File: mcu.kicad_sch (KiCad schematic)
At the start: 2 parts, among them U1 nRF52840

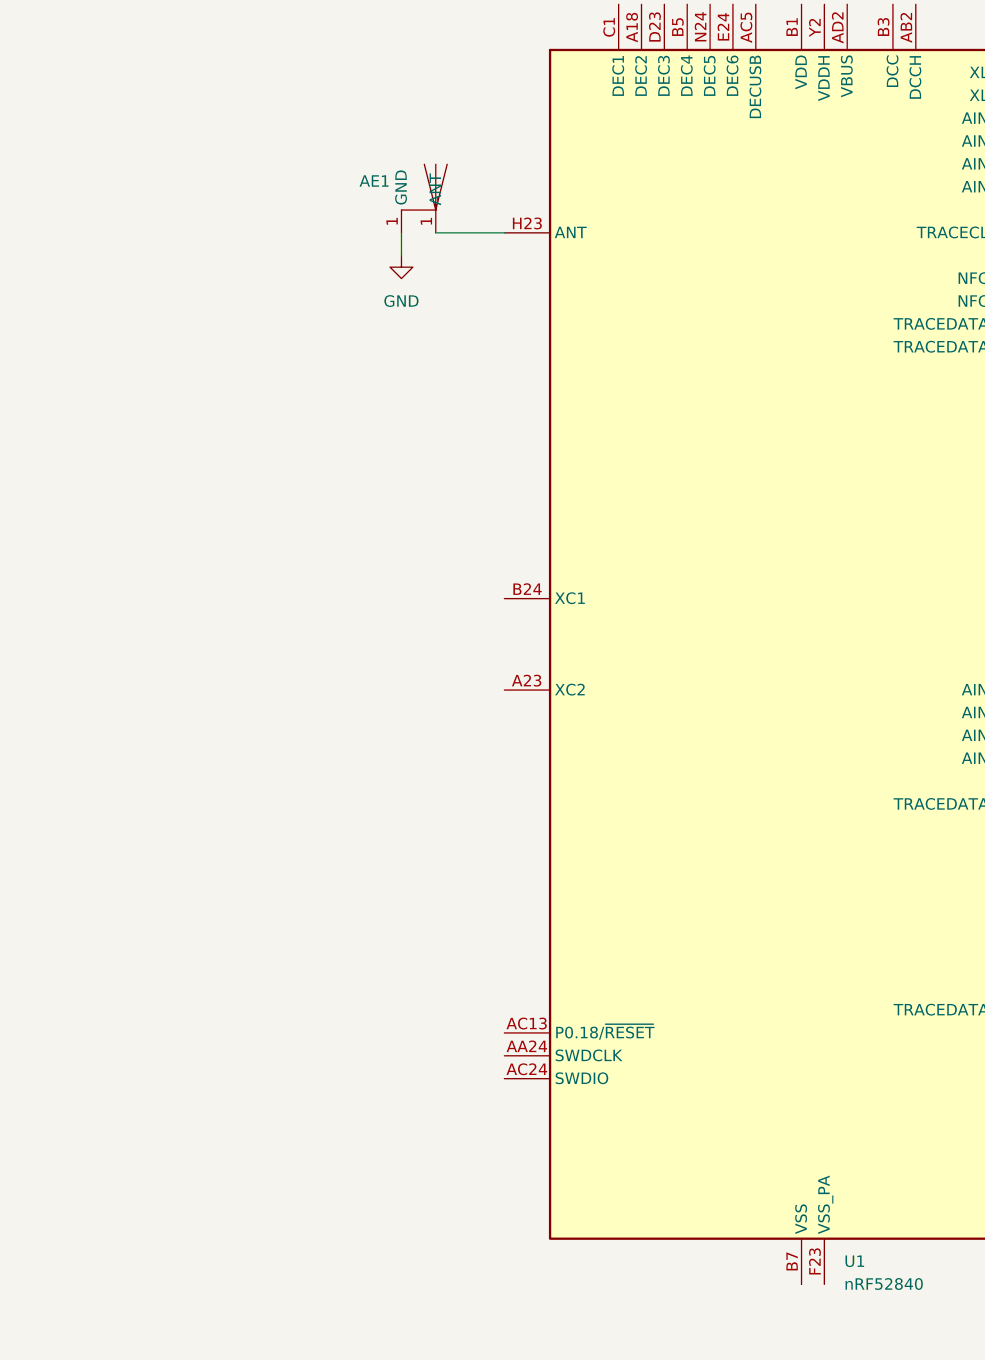
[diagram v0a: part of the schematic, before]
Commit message: Added antenna
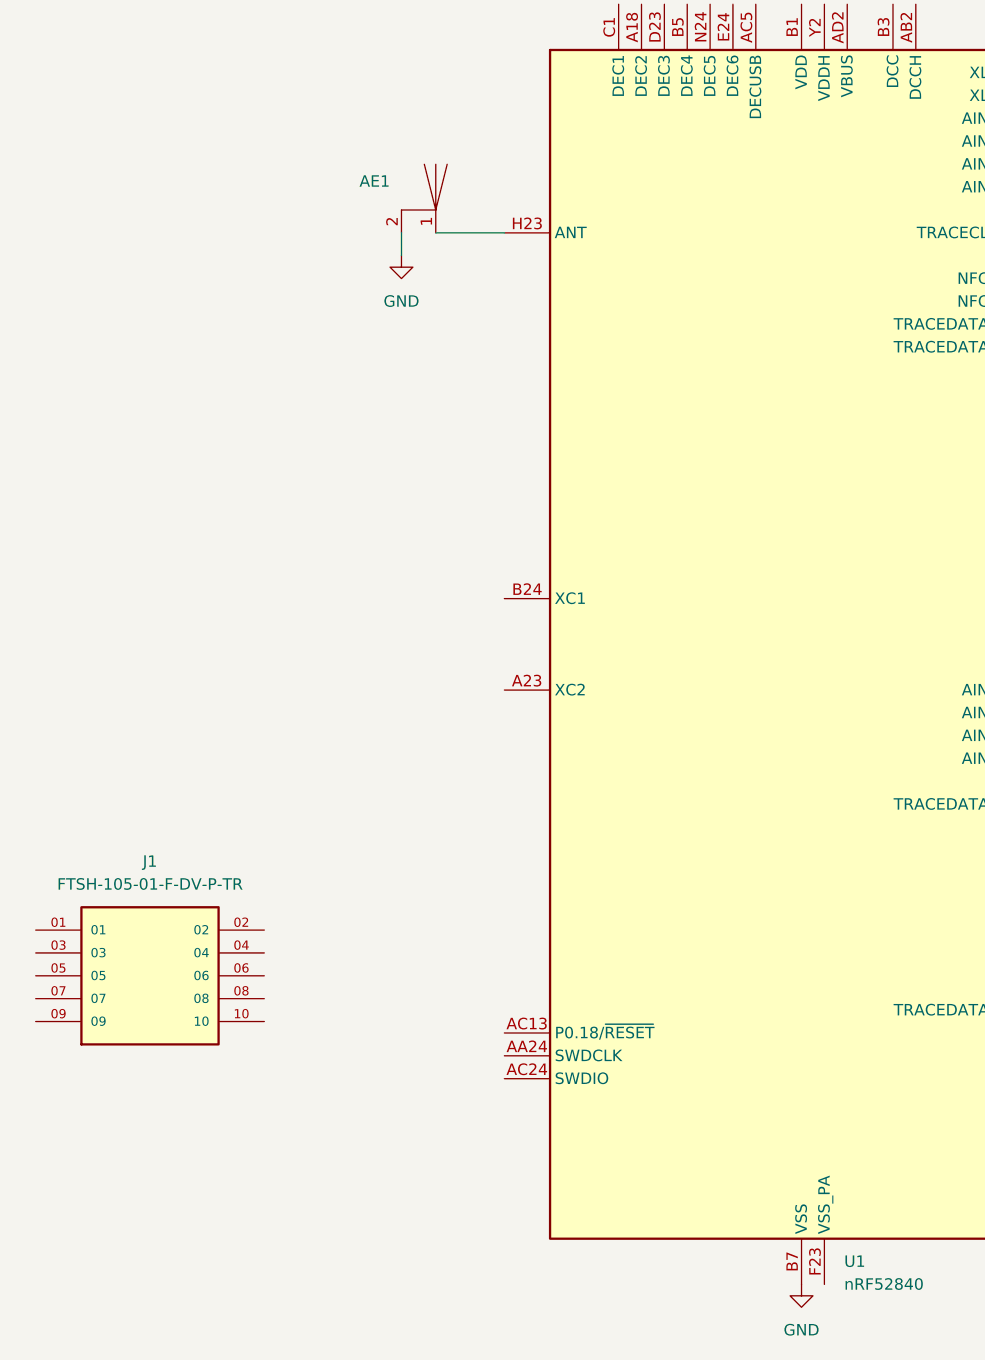
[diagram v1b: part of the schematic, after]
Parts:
- added J1: FTSH-105-01-F-DV-P-TR, Personal:SAMTEC_FTSH-105-01-F-DV-P-TR, symbol FTSH-105-01-F-DV-P-TR:FTSH-105-01-F-DV-P-TR
- AE1: now left out of the parts list
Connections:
- net GND: now also AE1.2, U1.B7 (VSS), U1.EP (VSS); no longer AE1.1 (GND)
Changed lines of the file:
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@@
+	)
+	(symbol
+		(lib_id "FTSH-105-01-F-DV-P-TR:FTSH-105-01-F-DV-P-TR")
+		(at 53.34 135.89 0)
+		(unit 1)
+		(exclude_from_sim no)
+		(in_bom yes)
+		(on_board yes)
+		(dnp no)
+		(fields_autoplaced yes)
+		(property "Reference" "J1"
+			(at 53.34 123.19 0)
+			(effects
+				(font
+					(size 1.27 1.27)
+				)
+			)
+		)
+		(property "Value" "FTSH-105-01-F-DV-P-TR"
+			(at 53.34 125.73 0)
+			(effects
+				(font
+					(size 1.27 1.27)
+				)
+			)
+		)
+		(property "Footprint" "Personal:SAMTEC_FTSH-105-01-F-DV-P-TR"
+			(at 53.34 135.89 0)
+			(effects
+				(font
+					(size 1.27 1.27)
+				)
+				(justify bottom)
+				(hide yes)
+			)
+		)
+		(property "Datasheet" ""
+			(at 53.34 135.89 0)
+			(effects
+				(font
+					(size 1.27 1.27)
+				)
+				(hide yes)
+			)
+		)
+		(property "Description" ""
+			(at 53.34 135.89 0)
+			(effects
+				(font
+					(size 1.27 1.27)
+				)
+				(hide yes)
+			)
+		)
+		(property "PARTREV" "R"
+			(at 53.34 135.89 0)
+			(effects
+				(font
+					(size 1.27 1.27)
+				)
+				(justify bottom)
+				(hide yes)
+			)
+		)
+		(property "MANUFACTURER" "Samtec"
+			(at 53.34 135.89 0)
+			(effects
+				(font
+					(size 1.27 1.27)
+				)
+				(justify bottom)
+				(hide yes)
+			)
+		)
+		(property "STANDARD" "Manufacturer Recommendations"
+			(at 53.34 135.89 0)
+			(effects
+				(font
+					(size 1.27 1.27)
+				)
+				(justify bottom)
+				(hide yes)
+			)
+		)
+		(pin "03"
+		)
+		(pin "04"
+		)
+		(pin "09"
+		)
+		(pin "10"
+		)
+		(pin "01"
+		)
+		(pin "05"
+		)
+		(pin "06"
+		)
+		(pin "07"
+		)
+		(pin "08"
+		)
+		(pin "02"
+		)
+		(instances
+			(project ""
+				(path "/4b478080-1b18-4cae-a6eb-51454cf43595/078ad315-b40f-432c-8194-3143ad5dab09"
+					(reference "J1")
+					(unit 1)
+				)
+			)
+		)
 	)
 	(symbol
@@
 	)
 	(symbol
+		(lib_id "power:GND")
+		(at 125.73 170.18 0)
+		(unit 1)
+		(exclude_from_sim no)
+		(in_bom yes)
+		(on_board yes)
+		(dnp no)
+		(fields_autoplaced yes)
+		(property "Reference" "#PWR02"
+			(at 125.73 176.53 0)
+			(effects
+				(font
+					(size 1.27 1.27)
+				)
+				(hide yes)
+			)
+		)
+		(property "Value" "GND"
+			(at 125.73 175.26 0)
+			(effects
+				(font
+					(size 1.27 1.27)
+				)
+			)
+		)
+		(property "Footprint" ""
+			(at 125.73 170.18 0)
+			(effects
+				(font
+					(size 1.27 1.27)
+				)
+				(hide yes)
+			)
+		)
+		(property "Datasheet" ""
+			(at 125.73 170.18 0)
+			(effects
+				(font
+					(size 1.27 1.27)
+				)
+				(hide yes)
+			)
+		)
+		(property "Description" "Power symbol creates a global label with name \"GND\" , ground"
+			(at 125.73 170.18 0)
+			(effects
+				(font
+					(size 1.27 1.27)
+				)
+				(hide yes)
+			)
+		)
+		(pin "1"
+		)
+		(instances
+			(project ""
+				(path "/4b478080-1b18-4cae-a6eb-51454cf43595/078ad315-b40f-432c-8194-3143ad5dab09"
+					(reference "#PWR02")
+					(unit 1)
+				)
+			)
+		)
+	)
+	(symbol
 		(lib_id "generic:Trace_Antenna")
 		(at 85.09 50.8 0)
@@
 		(unit 1)
 		(exclude_from_sim no)
-		(in_bom yes)
+		(in_bom no)
 		(on_board yes)
 		(dnp no)
@@
 		(pin "1"
 		)
-		(pin "1"
+		(pin "2"
 		)
 		(instances

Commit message: Setup charging
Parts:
- added C1, C2, C3, C4, C5, C6: C, symbol Device:C
- added L1: L, symbol Device:L
- added Y1: 32MHz, Crystal:Crystal_SMD_HC49-SD, symbol Device:Crystal
- added Y2: 32.768kHz, Crystal:Crystal_SMD_3215-2Pin_3.2x1.5mm, symbol Device:Crystal
- J1: LCSC PN (none) -> C5136979; Part Number (none) -> FTSH-105-01-F-DV-P-TR
- U1: LCSC PN (none) -> C190794; Part Number (none) -> NRF52840-QIAA-R
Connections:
- net GND: now also C1.1, C2.1, C3.2, C4.2
- net at J1.02: now also U1.AC24 (SWDIO)
- net at J1.04: now also U1.AA24 (SWDCLK)
- net at U1.A23 (XC2): now also C2.2, Y1.1
- net D-: now reaches U1.AD4 (D-)
- net D+: now reaches U1.AD6 (D+)
- net at U1.B24 (XC1): now also C1.2, Y1.2
- net at U1.D2 (XL1/P0.00): now also C3.1, Y2.2
- net at U1.F2 (XL2/P0.01): now also C4.1, Y2.1
- net at AE1.1: now also C5.1, L1.1; no longer U1.H23 (ANT)
- new net: C6.1, L1.2, U1.H23 (ANT)
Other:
- moved on the sheet: AE1, J1

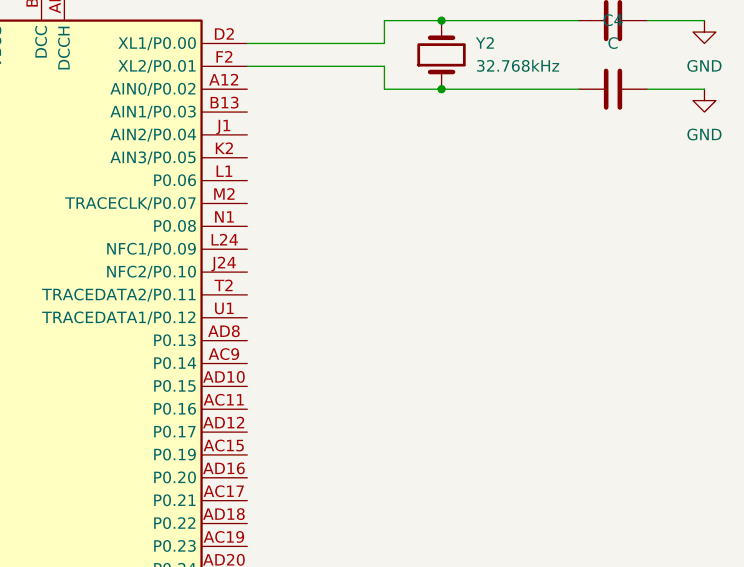
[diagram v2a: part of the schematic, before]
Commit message: Added outputs page
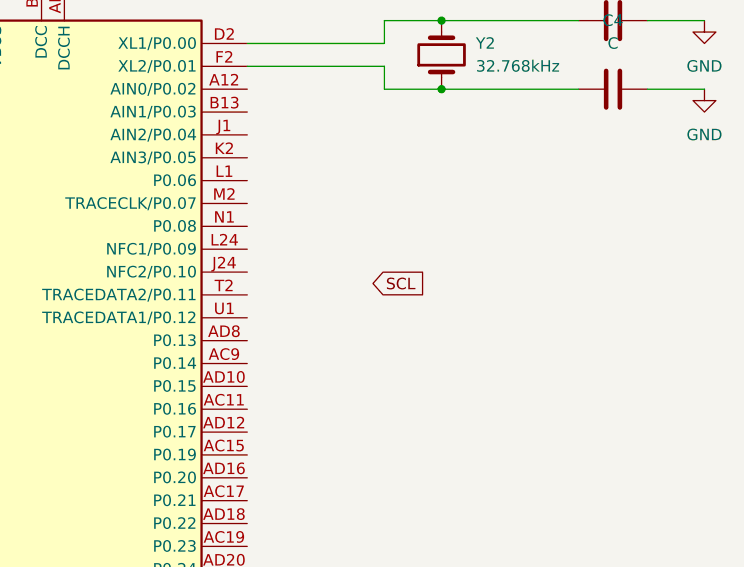
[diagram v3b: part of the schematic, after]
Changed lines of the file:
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@@
+		)
+	)
+	(global_label "SCL"
+		(shape input)
+		(at 172.72 62.23 0)
+		(fields_autoplaced yes)
+		(effects
+			(font
+				(size 1.27 1.27)
+			)
+			(justify left)
+		)
+		(property "Intersheetrefs" "${INTERSHEET_REFS}"
+			(at 179.2128 62.23 0)
+			(effects
+				(font
+					(size 1.27 1.27)
+				)
+				(justify left)
+				(hide yes)
+			)
 		)
 	)

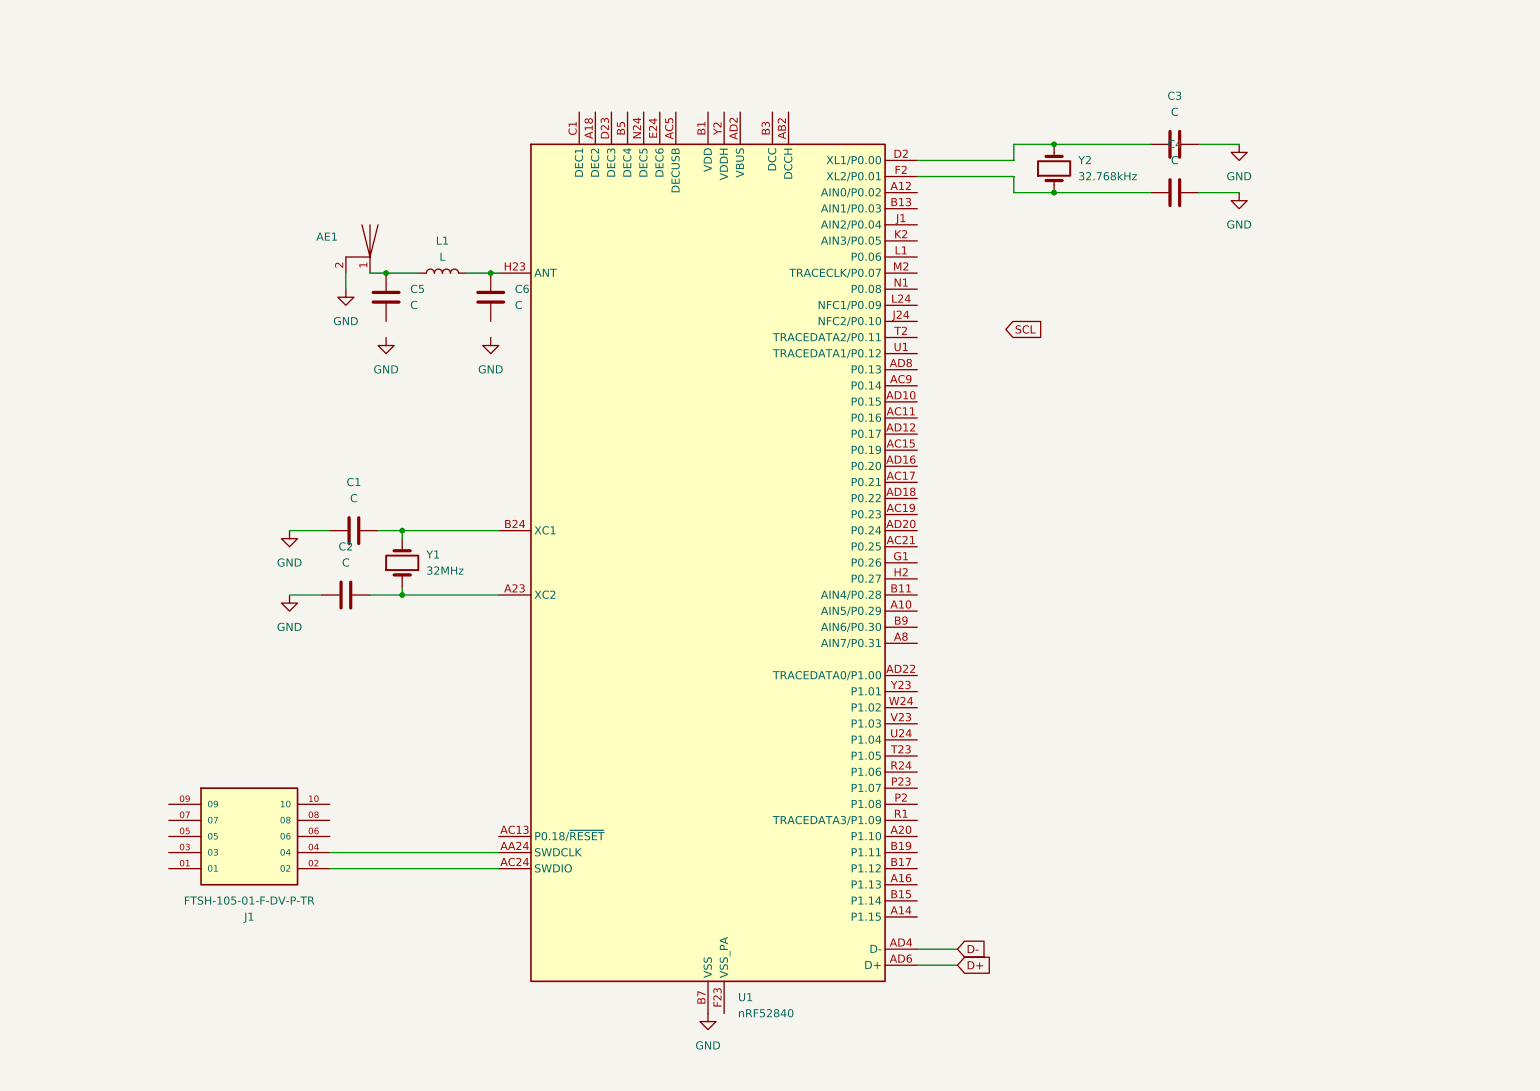
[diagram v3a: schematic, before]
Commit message: Added output headers
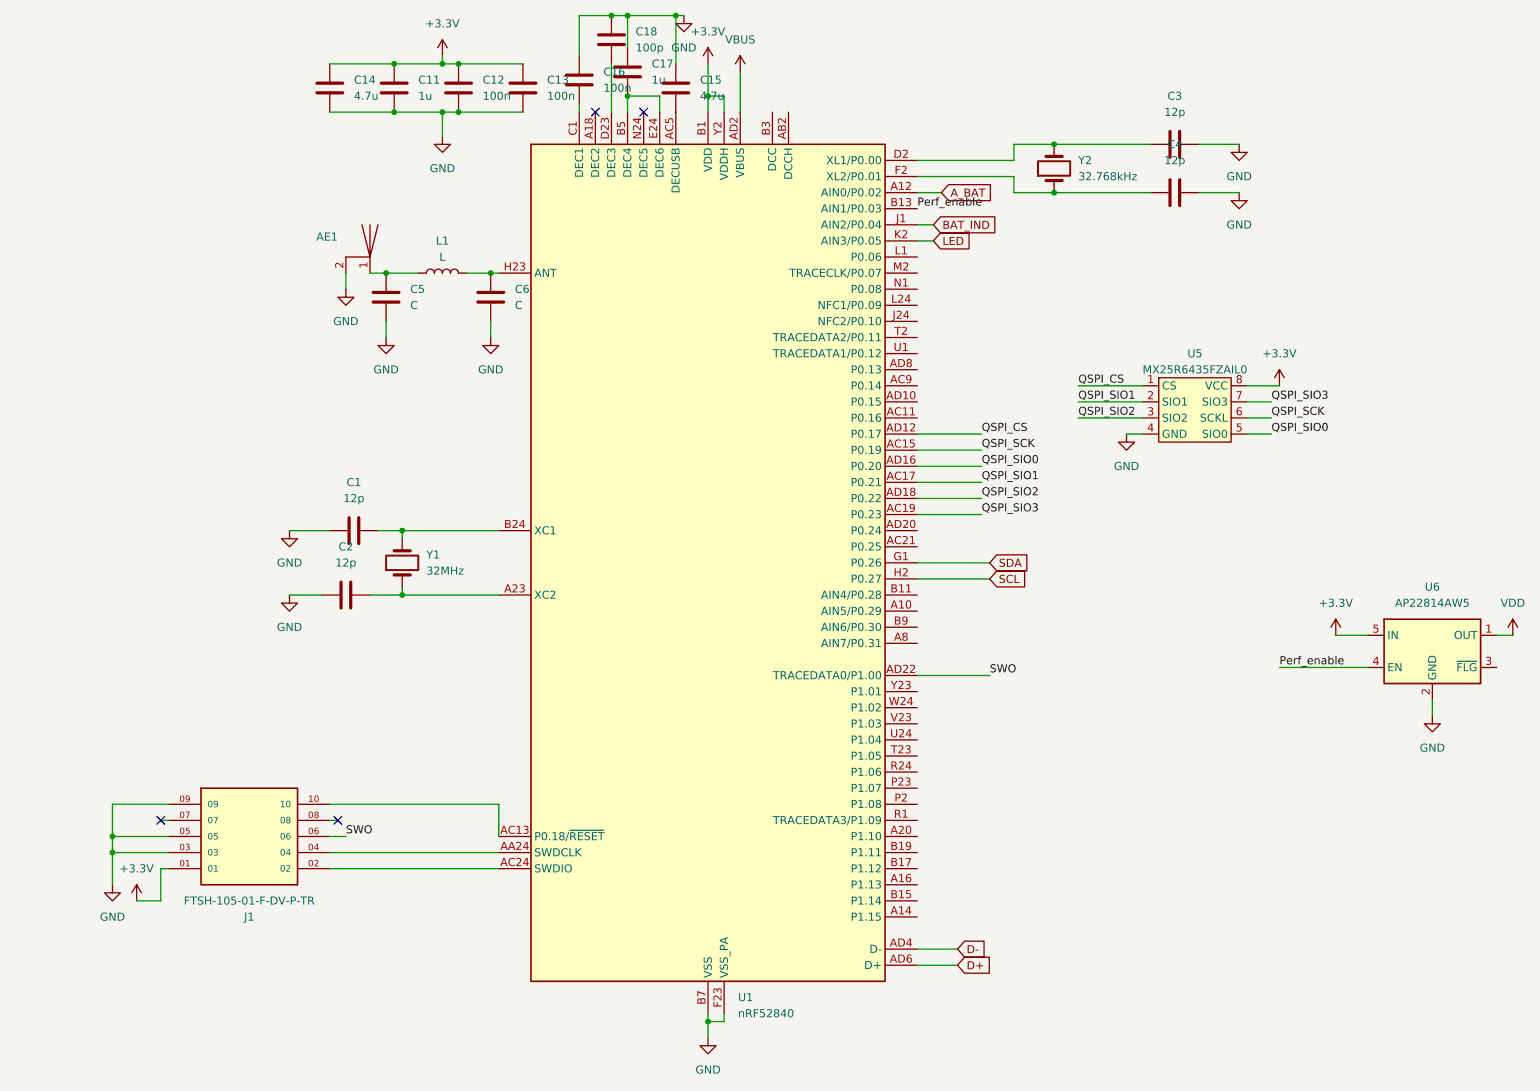
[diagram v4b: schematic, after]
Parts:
- added C11, C17: 1u, symbol Device:C
- added C12, C13, C16: 100n, symbol Device:C
- added C14, C15: 4.7u, symbol Device:C
- added C18: 100p, symbol Device:C
- added U5: MX25R6435FZAIL0, Package_SON:WSON-8-1EP_4x4mm_P0.8mm_EP1.98x3mm, symbol generic:MX25R6435FZAIL0
- added U6: AP22814AW5, Package_TO_SOT_SMD:SOT-23-5, symbol Power_Management:AP22814AW5
- C1, C2, C3, C4: value C -> 12p
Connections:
- net GND: now also C5.2, C6.2, J1.03, J1.05, J1.09, U1.F23 (VSS_PA), C11.2, C12.2, C13.2, C14.2, C15.2, C16.1, C17.1, C18.1, U5.4 (GND), U6.2 (GND)
- net SCL: now also U1.H2 (P0.27)
- net +3.3V: now reaches J1.01
- net +3.3V: now also U1.A22 (VDD), U1.AD14 (VDD), U1.AD23 (VDD), U1.B1 (VDD), U1.W1 (VDD), U1.Y2 (VDDH), C11.1, C12.1, C13.1, C14.1, U5.8 (VCC), U6.5 (IN)
- net SWO: now reaches J1.06
- net SWO: now also U1.AD22 (TRACEDATA0/P1.00)
- net at J1.10: now also U1.AC13 (P0.18/~{RESET})
- net A_BAT: now reaches U1.A12 (AIN0/P0.02)
- net QSPI_SCK: now reaches U1.AC15 (P0.19)
- net QSPI_SCK: now also U5.6 (SCKL)
- net QSPI_SIO1: now reaches U1.AC17 (P0.21)
- net QSPI_SIO1: now also U5.2 (SIO1)
- net QSPI_SIO3: now reaches U1.AC19 (P0.23)
- net QSPI_SIO3: now also U5.7 (SIO3)
- net at U1.AC5 (DECUSB): now also C15.1
- net QSPI_CS: now reaches U1.AD12 (P0.17)
- net QSPI_CS: now also U5.1 (CS)
- net QSPI_SIO0: now reaches U1.AD16 (P0.20)
- net QSPI_SIO0: now also U5.5 (SIO0)
- net QSPI_SIO2: now reaches U1.AD18 (P0.22)
- net QSPI_SIO2: now also U5.3 (SIO2)
- net VBUS: now reaches U1.AD2 (VBUS)
- net Perf_enable: now reaches U1.B13 (AIN1/P0.03)
- net Perf_enable: now also U6.4 (EN)
- net at U1.B5 (DEC4): now also U1.E24 (DEC6), C17.2
- net at U1.C1 (DEC1): now also C16.2
- net at U1.D23 (DEC3): now also C18.2
- net SDA: now reaches U1.G1 (P0.26)
- net BAT_IND: now reaches U1.J1 (AIN2/P0.04)
- net LED: now reaches U1.K2 (AIN3/P0.05)
- new net VDD: U6.1 (OUT)
- no-connect marks 0 -> 4
